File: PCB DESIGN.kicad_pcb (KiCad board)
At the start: 2 copper layers, 40 parts, among them J1 TYPE-C-31-M-12, J2 Conn_01x08_Pin, U1 AMS1117-3.3, U2 ESP32-S3-WROOM-1U-N16R8

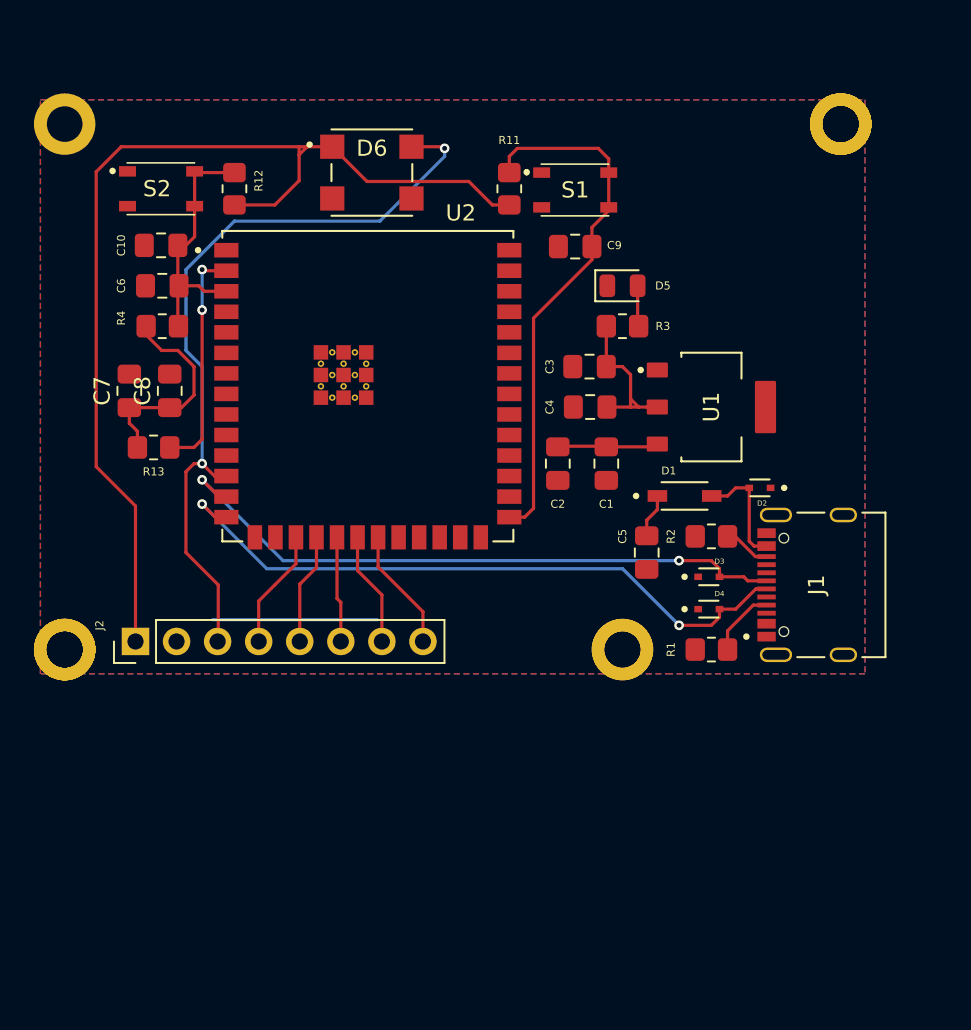
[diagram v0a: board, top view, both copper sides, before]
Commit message: footprint placement + schematic repair
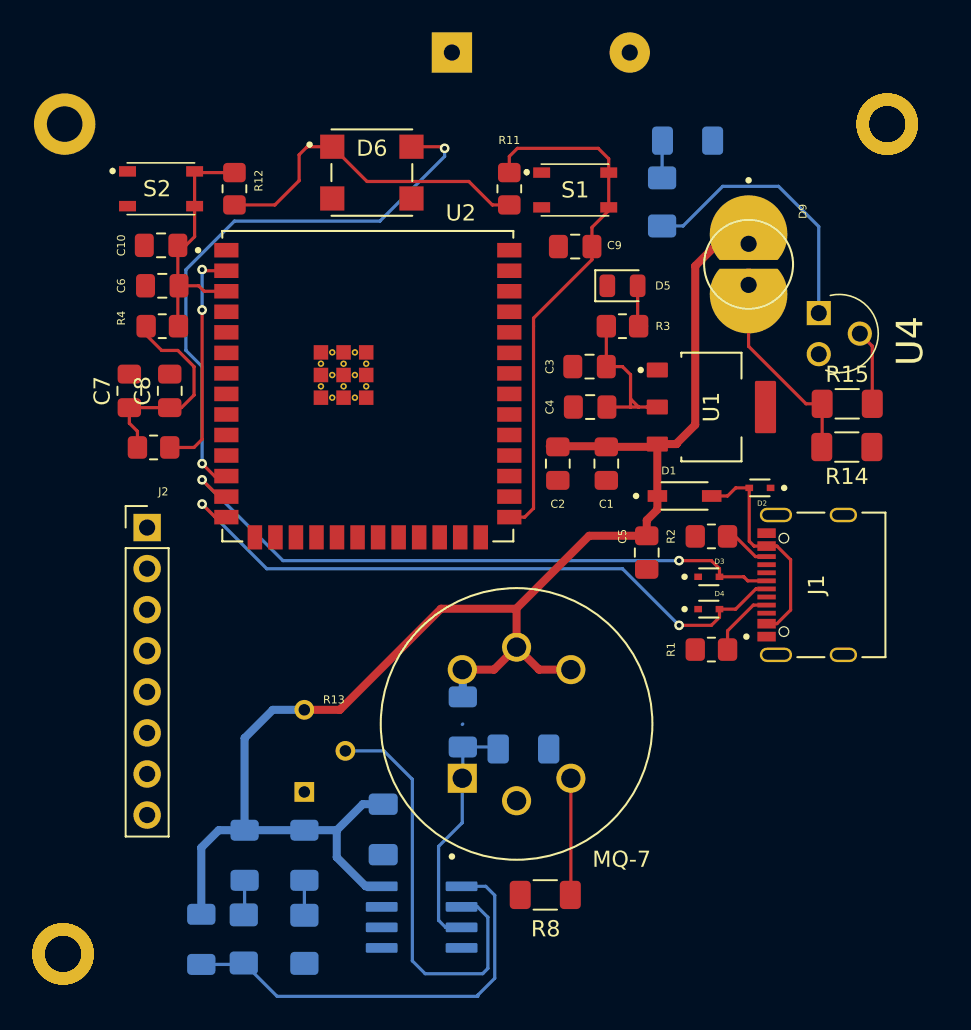
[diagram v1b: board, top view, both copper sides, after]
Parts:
- removed the ? at (150.0, 77.5)
- removed the REF** at (150.0, 77.5)
- added 3362P-1-503LF1: 3362P-1-503LF, footprints:TRIM_3362P-1-503LF, B.Cu at (130.3, 83.8)
- added C11: C, Capacitor_SMD:C_1206_3216Metric_Pad1.33x1.80mm_HandSolder, B.Cu at (135.2, 88.6)
- added C12: C, Capacitor_SMD:C_1206_3216Metric_Pad1.33x1.80mm_HandSolder, B.Cu at (143.9, 83.7)
- added D10: LED, LED_SMD:LED_1206_3216Metric_Pad1.42x1.75mm_HandSolder, B.Cu at (152.4, 49.8)
- added D7: LED, LED_SMD:LED_1206_3216Metric_Pad1.42x1.75mm_HandSolder, B.Cu at (126.6, 95.4)
- added D8: LED, LED_SMD:LED_1206_3216Metric_Pad1.42x1.75mm_HandSolder, B.Cu at (130.3, 95.4)
- added D9: SFH_4545, footprints:DIO_SFH_4545, F.Cu at (157.8, 53.7)
- added LM393AD1: LM393AD, footprints:SOIC127P599X175-8N, B.Cu at (137.6, 94.0)
- added LS1: CPI-3116-3-100T, footprints:XDCR_CPI-3116-3-100T, B.Cu at (144.9, 40.6)
- added MQ-7: MQ-7, footprints:XDCR_MQ-7, F.Cu at (143.4, 82.1)
- added R10: 220, Resistor_SMD:R_1206_3216Metric_Pad1.30x1.75mm_HandSolder, B.Cu at (154.0, 46.0)
- added R14: 220, Resistor_SMD:R_1206_3216Metric_Pad1.30x1.75mm_HandSolder, F.Cu at (163.9, 65.0)
- added R15: 220, Resistor_SMD:R_1206_3216Metric_Pad1.30x1.75mm_HandSolder, F.Cu at (163.9, 62.3)
- added R5: R, Resistor_SMD:R_1206_3216Metric_Pad1.30x1.75mm_HandSolder, B.Cu at (126.6, 90.2)
- added R6: R, Resistor_SMD:R_1206_3216Metric_Pad1.30x1.75mm_HandSolder, B.Cu at (130.3, 90.2)
- added R7: R, Resistor_SMD:R_1206_3216Metric_Pad1.30x1.75mm_HandSolder, B.Cu at (140.1, 82.0)
- added R8: R, Resistor_SMD:R_1206_3216Metric_Pad1.30x1.75mm_HandSolder, F.Cu at (145.2, 92.7)
- added R9: R, Resistor_SMD:R_1206_3216Metric_Pad1.30x1.75mm_HandSolder, B.Cu at (124.0, 95.4)
- added U4: BC547B, footprints:TO127P254X732-3, F.Cu at (164.7, 59.2)
- moved ? 70.3 mm to (115.4, 96.3) (x3)
- moved REF** 70.3 mm to (115.4, 96.3)
- moved ? 60.4 mm to (166.4, 45.0) (x3)
- moved REF** 60.4 mm to (166.4, 45.0)
- moved J2 7.08 mm to (120.6, 70.0), turned to 0 degrees
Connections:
- C1 pad 1: VCC_5V -> 5V
- C2 pad 1: VCC_5V -> 5V
- U1 pad 3: VCC_5V -> 5V
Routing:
- net 5V: track 2.74 -> 100.4 mm
- net VCC_3V3: track 65.2 -> 20.9 mm
- net OUT: track 0.00 -> 27.0 mm
- net Net-(LM393AD1-1IN-): track 0.00 -> 26.3 mm
- net BL: track 17.8 -> 0.00 mm
- net Net-(D10-A): track 0.00 -> 17.1 mm
- net A0: track 0.00 -> 15.2 mm
- net DIN: track 48.3 -> 35.7 mm
- net Net-(D9-PadA): track 0.00 -> 12.1 mm
- net CLK: track 7.39 -> 0.00 mm
- net Net-(MQ-7-B-Pad3): track 0.00 -> 7.23 mm
- net RST: track 7.06 -> 0.00 mm
- net CS: track 6.87 -> 0.00 mm
- net Net-(D1-PadA): track 7.02 -> 13.8 mm
- net VCC_5V: track 6.74 -> 0.00 mm
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- removed copper zone on B.Cu, net GND
- removed copper zone on F.Cu, net GND
